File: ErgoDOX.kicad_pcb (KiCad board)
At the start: 2 copper layers, 182.8 x 158.9 mm, 101 parts, among them J1 USB, J2 3.5mm, J3 JMP, J4 JMP, SW1 SWITCH_PUSH, SW10 SWITCH_PUSH, SW11 SWITCH_PUSH, SW12 SWITCH_PUSH, SW13 SWITCH_PUSH, SW14 SWITCH_PUSH, SW15 SWITCH_PUSH, SW16 SWITCH_PUSH, SW17 SWITCH_PUSH, SW18 SWITCH_PUSH, SW19 SWITCH_PUSH, SW2 SWITCH_PUSH, SW20 SWITCH_PUSH, SW21 SWITCH_PUSH, SW22 SWITCH_PUSH, SW23 SWITCH_PUSH, SW24 SWITCH_PUSH, SW25 SWITCH_PUSH, SW26 SWITCH_PUSH, SW27 SWITCH_PUSH, SW28 SWITCH_PUSH, SW29 SWITCH_PUSH, SW3 SWITCH_PUSH, SW30 SWITCH_PUSH, SW31 SWITCH_PUSH, SW32 SWITCH_PUSH, SW33 SWITCH_PUSH, SW34 SWITCH_PUSH, SW35 SWITCH_PUSH, SW36 SWITCH_PUSH, SW37 SWITCH_PUSH, SW38 SWITCH_PUSH, SW39 SWITCH_PUSH, SW4 SWITCH_PUSH, SW40 SWITCH_PUSH, SW41 SWITCH_PUSH, SW42 SWITCH_PUSH, SW43 SWITCH_PUSH, SW44 SWITCH_PUSH, SW5 SWITCH_PUSH, SW6 SWITCH_PUSH, SW7 SWITCH_PUSH, SW8 SWITCH_PUSH, SW9 SWITCH_PUSH, U1 ProMicro

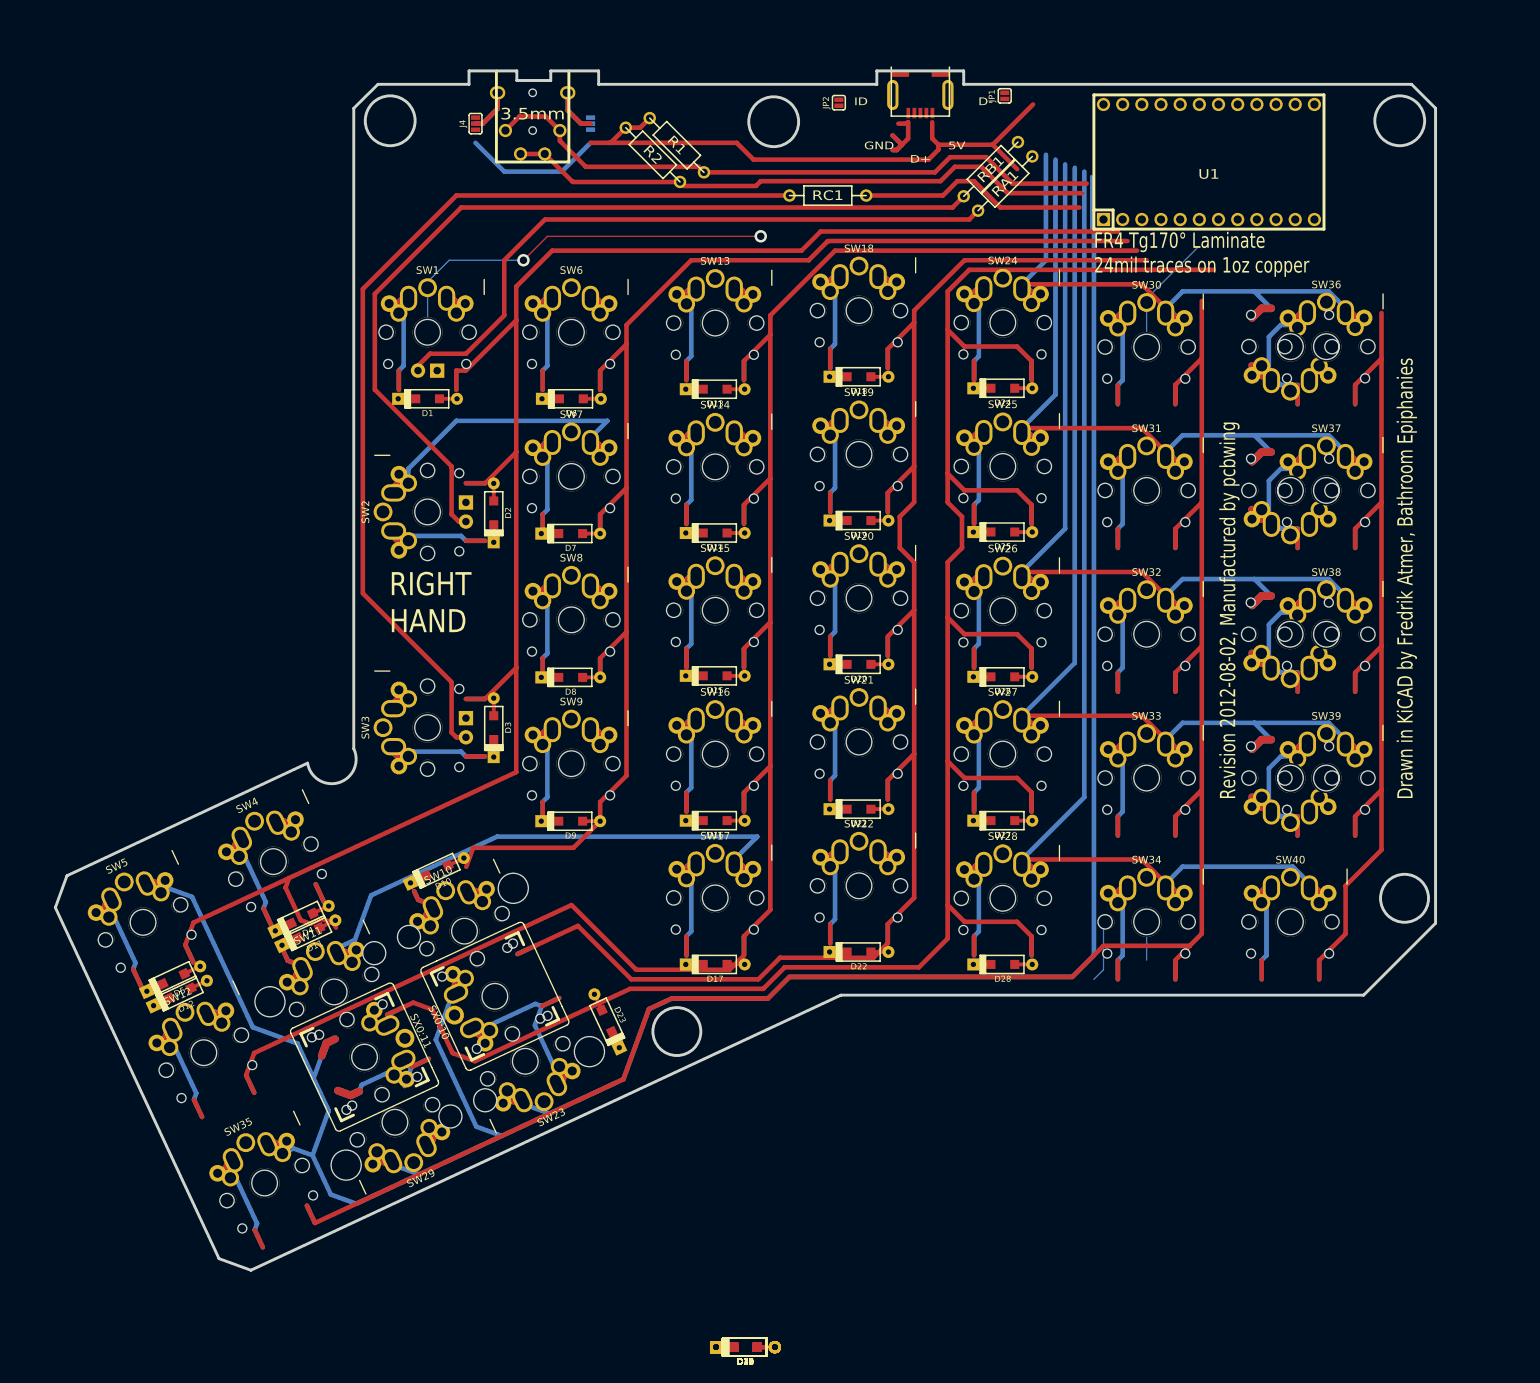
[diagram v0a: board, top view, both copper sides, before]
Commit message: component placement
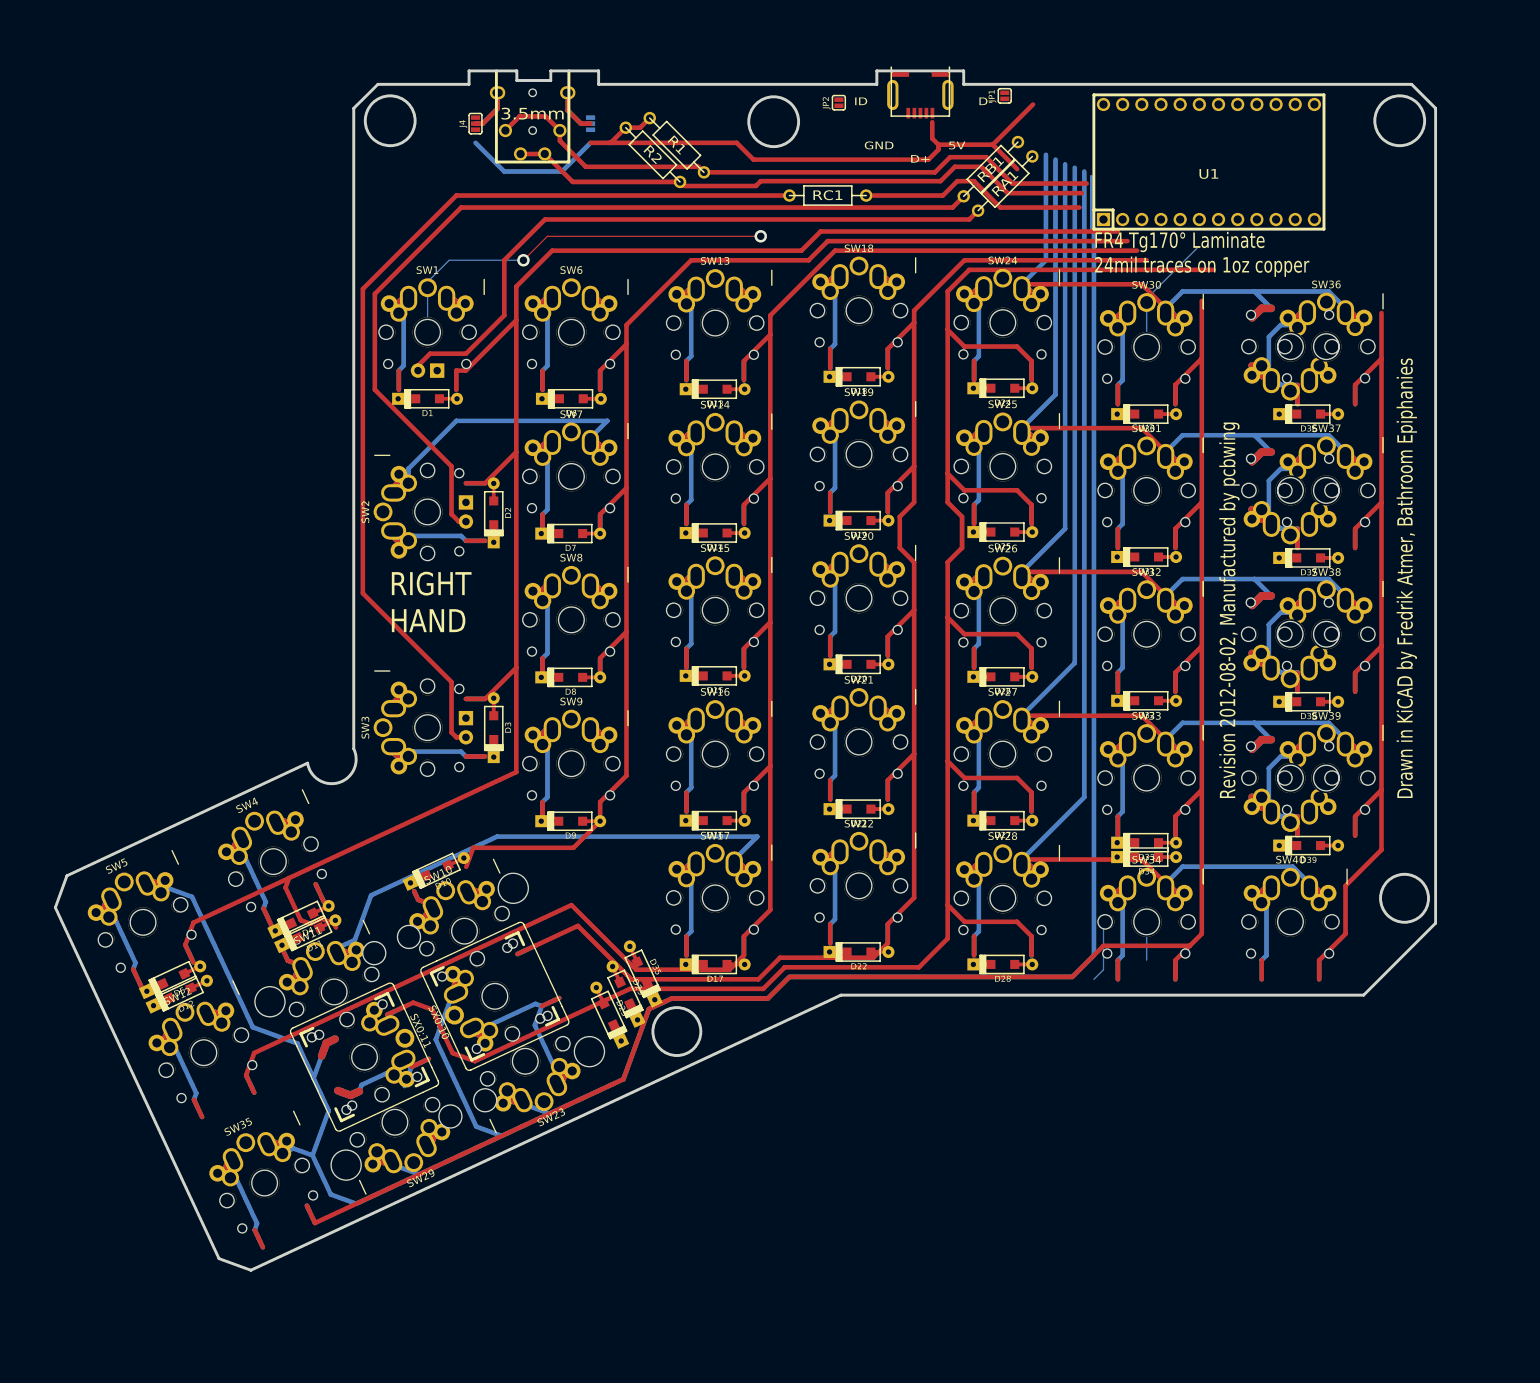
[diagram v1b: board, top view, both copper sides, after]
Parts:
- removed D40: DIODE, BishopKicadConsolidated:D_SOD123_axial
- moved D36 144.4 mm to (189.1, 75.9)
- moved D30 134.5 mm to (167.6, 75.9)
- moved D37 128.4 mm to (189.1, 95.0)
- moved D31 117.4 mm to (167.6, 94.9)
- moved D38 113.5 mm to (189.1, 114.0)
- moved D32 100.8 mm to (167.6, 113.9)
- moved D39 99.9 mm to (189.1, 133.1)
- moved D33 85.4 mm to (167.6, 132.7)
- moved D34 83.9 mm to (167.6, 134.6)
- moved D35 51.4 mm to (100.8, 150.0), turned to 115 degrees
- moved D29 49.5 mm to (98.6, 152.7), turned to 115 degrees
- moved D23 0.92 mm to (96.4, 155.4)
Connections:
- SW30 pad 2: Net-(SW30-Pad2) -> Net-(D30-Pad1)
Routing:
- net Net-(SW30-Pad2): track 16.8 -> 0.00 mm
- net Net-(D30-Pad1): track 0.00 -> 16.8 mm
- net (no net): track 1353.7 -> 1342.5 mm

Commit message: removed old traces
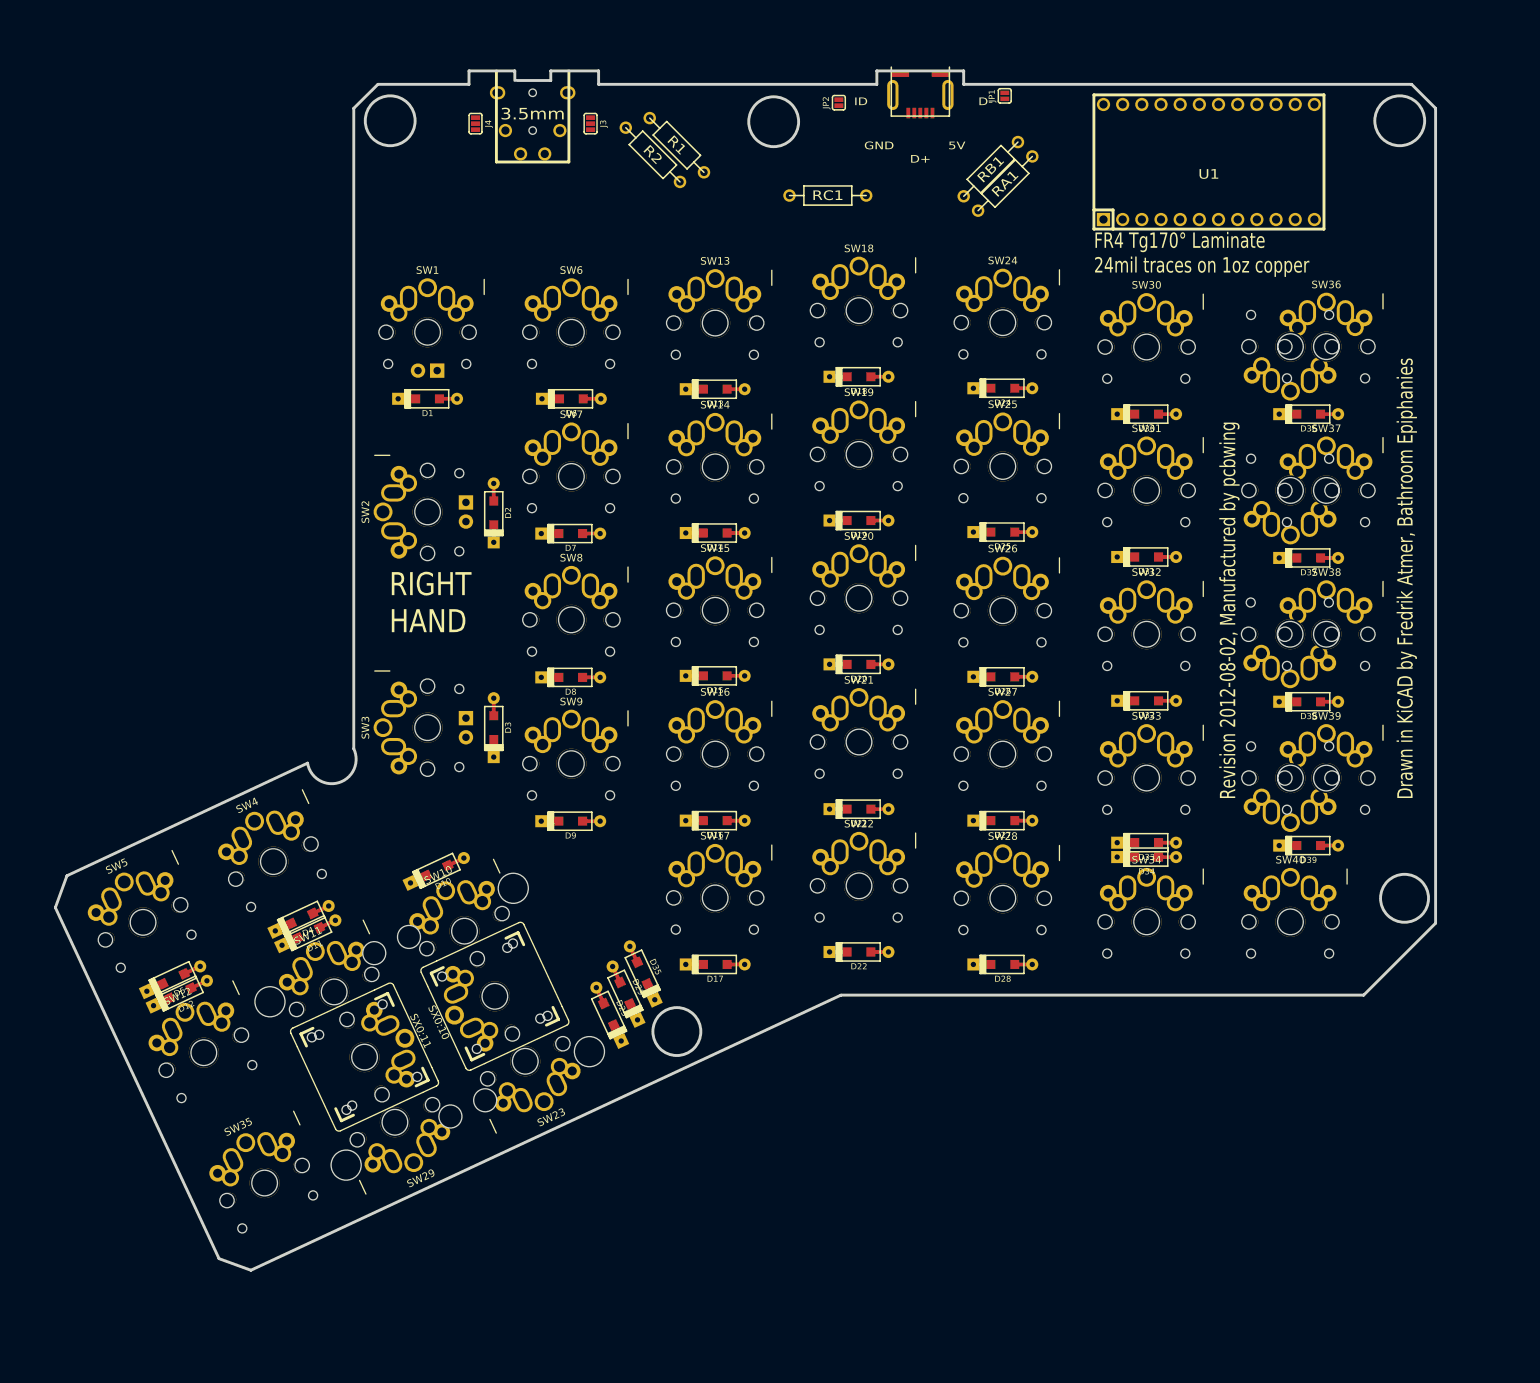
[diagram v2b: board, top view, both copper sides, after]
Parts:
- J3: moved to F.Cu
- turned J3 to 270 degrees
- turned J4 to 270 degrees
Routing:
- net (no net): track 1342.5 -> 0.00 mm
- net /ROW0: track 435.0 -> 0.00 mm
- net /COL5: track 428.0 -> 0.00 mm
- net /ROW5: track 182.8 -> 0.00 mm, vias 2 -> 0
- net /ROW1: track 178.8 -> 0.00 mm
- net /ROW2: track 170.7 -> 0.00 mm
- net /ROW4: track 166.7 -> 0.00 mm
- net /ROW3: track 145.4 -> 0.00 mm
- net Net-(LED_C1-Pad1): track 127.4 -> 0.00 mm
- net Net-(LED_B1-Pad1): track 119.1 -> 0.00 mm
- net Net-(LED_A1-Pad1): track 87.6 -> 0.00 mm
- net /SDAM: track 83.9 -> 0.00 mm
- net /SCLM: track 78.6 -> 0.00 mm
- net VCC: track 77.5 -> 0.00 mm
- net Net-(D23-Pad1): track 32.3 -> 0.00 mm
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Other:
- outline, holes or cut-outs redrawn

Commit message: component placement circuit mod
replicated the Let's split cirucit design to this project. finilized placement of the initial components
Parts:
- added D40: DIODE, BishopKicadConsolidated:D_SOD123_axial, F.Cu at (177.0, 143.3)
- added J5: JMP, BishopKicadConsolidated:SOLDER_JUMPER_3, B.Cu at (78.7, 37.5)
- added J6: JMP, BishopKicadConsolidated:SOLDER_JUMPER_3, B.Cu at (94.0, 37.5)
- added SW45: SWITCH_PUSH, BishopKicadConsolidated:SOLDER_JUMPER_2, F.Cu at (156.3, 32.6)
- added SW46: SWITCH_PUSH, BishopKicadConsolidated:SOLDER_JUMPER_2, B.Cu at (156.3, 32.6)
- added W1: TEST_1P, BishopKicadConsolidated:PIN_1, F.Cu at (86.4, 46.2)
- added W2: TEST_1P, BishopKicadConsolidated:PIN_1, F.Cu at (103.8, 40.9)
- added W3: TEST_1P, BishopKicadConsolidated:PIN_1, F.Cu at (201.2, 45.5)
- added W4: TEST_1P, BishopKicadConsolidated:PIN_1, F.Cu at (201.2, 47.8)
- added W5: TEST_1P, BishopKicadConsolidated:PIN_1, F.Cu at (201.2, 50.0)
- moved D34 9.92 mm to (158.0, 136.9), turned to 90 degrees
- moved D39 0.64 mm to (188.5, 133.1)
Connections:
- J2 pad 2: /SDAM -> /DATA
- J2 pad 3: /SCLM -> /XTRADATA
- J2 pad 5: /SCLM -> /XTRADATA
- J2 pad 6: /SDAM -> /DATA
- J3 pad 1: VCC -> GND
- J3 pad 3: GND -> VCC
- J4 pad 1: VCC -> GND
- J4 pad 3: GND -> VCC
- R1 pad 2: /SDAM -> (no net)
- R2 pad 2: /SCLM -> /XTRADATA
- RA1 pad 1: /LED_A -> (no net)
- RB1 pad 1: /LED_B -> (no net)
- RC1 pad 1: /LED_C -> (no net)
- U1 pad 10: /COL5 -> /COL4
- U1 pad 11: /COL6 -> /COL5
- U1 pad 12: /LED_A -> /COL6
- U1 pad 13: /SCLM -> Net-(U1-Pad13)
- U1 pad 14: /SDAM -> Net-(U1-Pad14)
- U1 pad 17: /LED_C -> /XTRADATA
- U1 pad 18: /LED_B -> /DATA
- U1 pad 3: (no net) -> Net-(SW45-Pad1)
- U1 pad 5: /COL0 -> Net-(U1-Pad5)
- U1 pad 6: /COL1 -> /COL0
- U1 pad 7: /COL2 -> /COL1
- U1 pad 8: /COL3 -> /COL2
- U1 pad 9: /COL4 -> /COL3
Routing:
- added copper zone on B.Cu, net GND
- added copper zone on F.Cu, net GND
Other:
- outline, holes or cut-outs redrawn
- board text added: "LEFT PAW"
- board text added: "RIGHT PAW"
- board text removed: "5V"
- board text removed: "D+"
- board text removed: "D-"
- board text removed: "Design by Dominic Beauchamp, based on the Key64 by Nestor A. Diaz"
- board text removed: "Drawn in KiCAD by Fredrik Atmer, Bathroom Epiphanies"
- board text removed: "FR4 Tg170° Laminate 24mil traces on 1oz copper"
- board text removed: "GND"
- board text removed: "ID"
- board text removed: "LEFT HAND"
- board text removed: "RIGHT HAND"
- board text removed: "Revision 2012-08-02, Manufactured by pcbwing"

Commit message: added unicorns
people love unicorns
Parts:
- added G***: LOGO, Silks:BKB small chess, F.Cu at (81.8, 72.1)
- added G***: LOGO, Silks:uUnicorn, F.Cu at (90.7, 138.2)
- added REF**: KiCAD Logo, Symbols:Symbol_KiCAD-Logo_CopperAndSilkScreenTop, F.Cu at (69.1, 42.9)
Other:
- board text added: "ErgoDox 2.0"
- board text added: "R0v1 05222018"
- board text added: "Re-Design By MrBishop of Bishop Keyboards 2018"
